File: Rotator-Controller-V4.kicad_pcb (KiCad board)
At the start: 2 copper layers, 99 x 70 mm, 91 parts, among them J1 Serial, J2 Rotator, J3 USB-C 2.0 16P, J4 Motor Cap, J6 Header 1x3, SW1 CW, SW2 CW, U1 ATtiny1616-M, U2 AP2161W, U3 CPC1966, U4 CPC1966, U5 CPC1966, U6 ADUM3160, U7 FT231XQ, U8 NDP6802SF-50

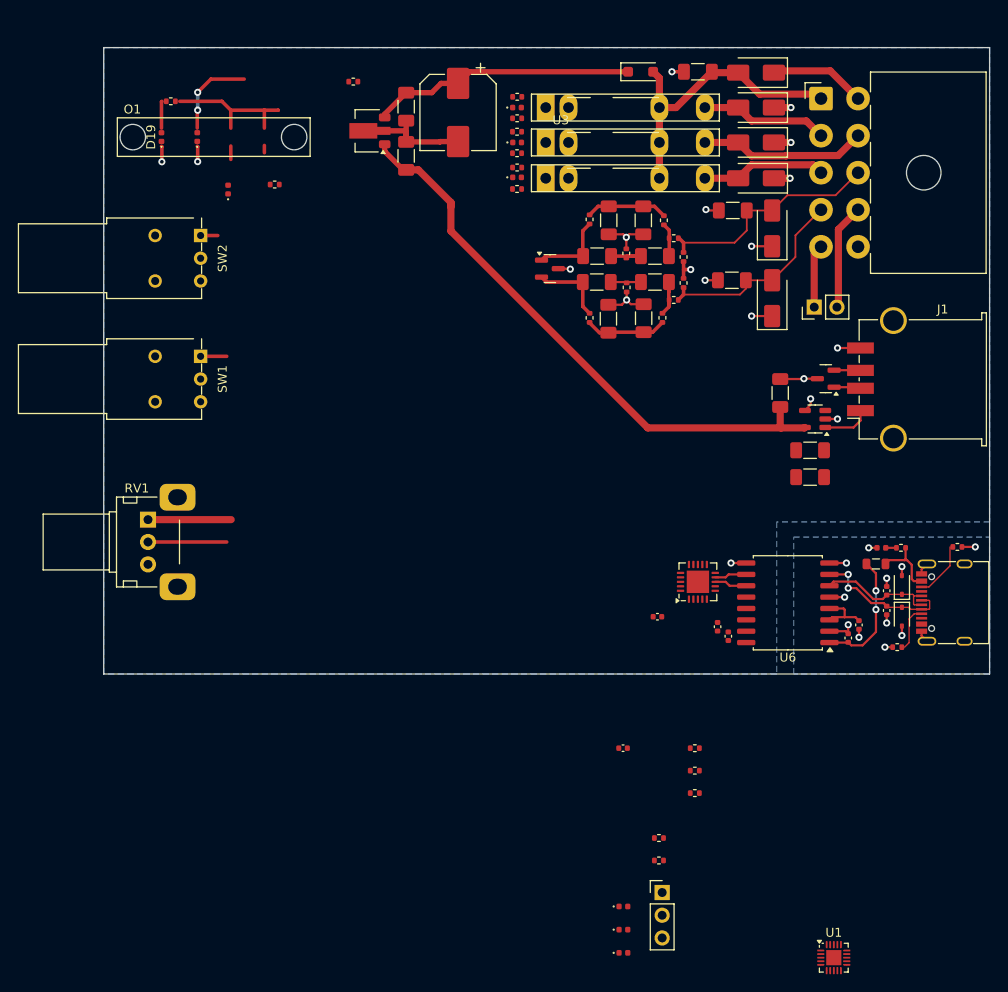
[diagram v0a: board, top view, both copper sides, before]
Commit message: More work on schematic Started software conversion to STM32F405 MCU
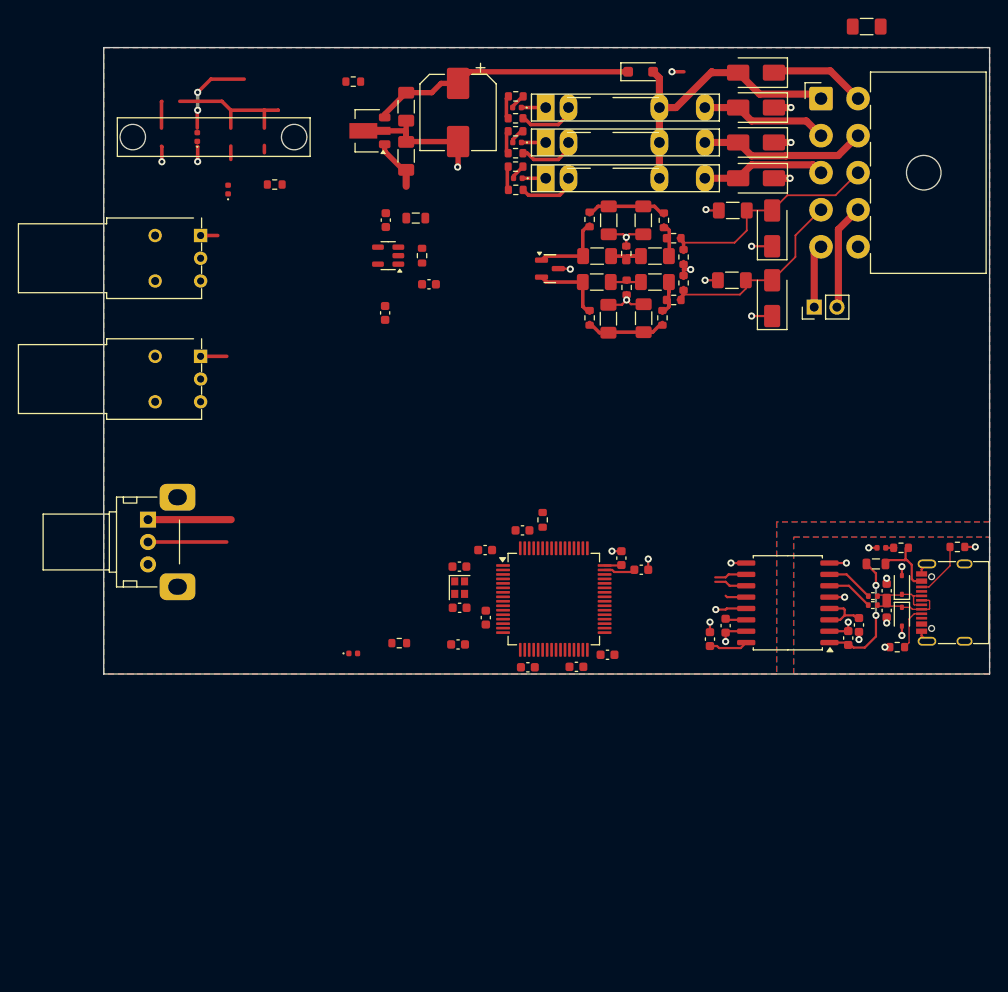
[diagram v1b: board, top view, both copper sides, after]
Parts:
- removed the C1 at (161.4, 57.7)
- removed the C19 at (156.9, 118.6)
- removed D19: 5V, LED_SMD:LED_0402_1005Metric
- removed D20, D21: Yellow, LED_SMD:LED_0402_1005Metric
- removed the D9 at (175.7, 92.0)
- removed the J1 at (185.9, 92.1)
- removed J6: Header 1x3, Connector_PinHeader_2.54mm:PinHeader_1x03_P2.54mm_Vertical
- removed the R15 at (102.5, 61.0)
- removed R27, R28, R29: 1K, Resistor_SMD:R_0402_1005Metric
- removed the U1 at (176.6, 156.7)
- added C11: 1u, Capacitor_SMD:C_0603_1608Metric, F.Cu at (141.8, 109.0)
- added C12: 10u, Capacitor_SMD:C_0603_1608Metric, F.Cu at (151.3, 122.8)
- added C16: 1u, Capacitor_SMD:C_0603_1608Metric, F.Cu at (152.8, 112.0)
- added C17: 10u, Capacitor_SMD:C_0603_1608Metric, F.Cu at (126.5, 74.3)
- added C18: 0.1u, Capacitor_SMD:C_0603_1608Metric, F.Cu at (137.7, 118.7)
- added C29: 0.1 200V, Capacitor_SMD:C_1206_3216Metric_Pad1.33x1.80mm_HandSolder, F.Cu at (180.3, 52.6)
- added C33: 10u, Capacitor_SMD:C_0603_1608Metric, F.Cu at (126.5, 84.7)
- added C34: 1u, Capacitor_SMD:C_0603_1608Metric, F.Cu at (131.3, 81.5)
- added C5: 10u, Capacitor_SMD:C_0603_1608Metric, F.Cu at (134.6, 121.7)
- added C6: 0.1u, Capacitor_SMD:C_0603_1608Metric, F.Cu at (137.6, 111.2)
- added C8: 1u, Capacitor_SMD:C_0603_1608Metric, F.Cu at (142.4, 124.2)
- added FB2: FerriteBead_Small, Inductor_SMD:L_0805_2012Metric, F.Cu at (129.9, 74.0)
- added R5: 27, Resistor_SMD:R_0402_1005Metric, F.Cu at (180.9, 117.3)
- added R6: 27, Resistor_SMD:R_0402_1005Metric, F.Cu at (181.0, 116.3)
- added R8: 10K, Resistor_SMD:R_0603_1608Metric, F.Cu at (144.1, 107.8)
- added Y1: 12M, Crystal:Crystal_SMD_2016-4Pin_2.0x1.6mm, F.Cu at (134.8, 115.3)
- C1: renamed from C16; footprint Capacitor_SMD:C_0402_1005Metric -> Capacitor_SMD:C_0603_1608Metric
- C10, C13: value 0.1 -> 20p; footprint Capacitor_SMD:C_1206_3216Metric_Pad1.33x1.80mm_HandSolder -> Capacitor_SMD:C_0603_1608Metric
- C14: value 120u -> 1u; footprint Capacitor_SMD:C_1206_3216Metric_Pad1.33x1.80mm_HandSolder -> Capacitor_SMD:C_0603_1608Metric
- C15: value .1u -> 10u; footprint Capacitor_SMD:C_0402_1005Metric -> Capacitor_SMD:C_0603_1608Metric
- C2: renamed from C20; footprint Capacitor_SMD:C_0402_1005Metric -> Capacitor_SMD:C_0603_1608Metric
- C3: renamed from C18; footprint Capacitor_SMD:C_0402_1005Metric -> Capacitor_SMD:C_0603_1608Metric
- C4: renamed from C25; footprint Capacitor_SMD:C_0402_1005Metric -> Capacitor_SMD:C_0603_1608Metric
- C7: renamed from C24; footprint Capacitor_SMD:C_0402_1005Metric -> Capacitor_SMD:C_0603_1608Metric
- C9: renamed from C17; footprint Capacitor_SMD:C_0402_1005Metric -> Capacitor_SMD:C_0603_1608Metric
- D16: renamed from D14; value SMAJ90CA -> SMAJ10CA
- D17: renamed from D15; value SMAJ90CA -> SMAJ10CA
- D4: renamed from D10; value White -> 5V_GRN
- R1: renamed from R10; footprint Resistor_SMD:R_0402_1005Metric -> Resistor_SMD:R_0603_1608Metric
- R10: renamed from R5; footprint Resistor_SMD:R_0402_1005Metric -> Resistor_SMD:R_0603_1608Metric
- R11: renamed from R20; value 1K5 -> 1K; footprint Resistor_SMD:R_0402_1005Metric -> Resistor_SMD:R_0603_1608Metric
- R12: renamed from R3; value 1k5 -> 1k; footprint Resistor_SMD:R_0402_1005Metric -> Resistor_SMD:R_0603_1608Metric
- R13: renamed from R19; value 1K5 -> 1K; footprint Resistor_SMD:R_0402_1005Metric -> Resistor_SMD:R_0603_1608Metric
- R14: renamed from R16; value 1K5 -> 1K; footprint Resistor_SMD:R_0402_1005Metric -> Resistor_SMD:R_0603_1608Metric
- R15: renamed from R18; value 1K5 -> 1K; footprint Resistor_SMD:R_0402_1005Metric -> Resistor_SMD:R_0603_1608Metric
- R16: renamed from R17; value 1K5 -> 1K; footprint Resistor_SMD:R_0402_1005Metric -> Resistor_SMD:R_0603_1608Metric
- R17: renamed from R1; footprint Resistor_SMD:R_0402_1005Metric -> Resistor_SMD:R_0603_1608Metric
- R18: renamed from R6; footprint Resistor_SMD:R_0402_1005Metric -> Resistor_SMD:R_0603_1608Metric
- R19: renamed from R8; footprint Resistor_SMD:R_0402_1005Metric -> Resistor_SMD:R_0603_1608Metric
- R2: renamed from R21; footprint Resistor_SMD:R_0402_1005Metric -> Resistor_SMD:R_0603_1608Metric
- R20: renamed from R7; footprint Resistor_SMD:R_0402_1005Metric -> Resistor_SMD:R_0603_1608Metric
- R21: renamed from R9; footprint Resistor_SMD:R_0402_1005Metric -> Resistor_SMD:R_0603_1608Metric
- R22: renamed from R11; footprint Resistor_SMD:R_0402_1005Metric -> Resistor_SMD:R_0603_1608Metric
- R23: renamed from R12; footprint Resistor_SMD:R_0402_1005Metric -> Resistor_SMD:R_0603_1608Metric
- R24: renamed from R13; footprint Resistor_SMD:R_0402_1005Metric -> Resistor_SMD:R_0603_1608Metric
- R25: renamed from R14; footprint Resistor_SMD:R_0402_1005Metric -> Resistor_SMD:R_0603_1608Metric
- R26: value 1K -> 10K; footprint Resistor_SMD:R_0402_1005Metric -> Resistor_SMD:R_0603_1608Metric
- R3: renamed from R22; footprint Resistor_SMD:R_0402_1005Metric -> Resistor_SMD:R_0603_1608Metric
- R4: renamed from R2; footprint Resistor_SMD:R_0402_1005Metric -> Resistor_SMD:R_0603_1608Metric
- R7: renamed from R25; footprint Resistor_SMD:R_0402_1005Metric -> Resistor_SMD:R_0603_1608Metric
- R9: renamed from R4; footprint Resistor_SMD:R_0402_1005Metric -> Resistor_SMD:R_0603_1608Metric
- U2: value AP2161W -> STM32F405RGTx; footprint Package_TO_SOT_SMD:SOT-23-5 -> Package_QFP:LQFP-64_10x10mm_P0.5mm
- U7: value FT231XQ -> AP2112K-3.3; footprint Package_DFN_QFN:QFN-20-1EP_4x4mm_P0.5mm_EP2.5x2.5mm -> Package_TO_SOT_SMD:SOT-23-5
- moved R26 72.6 mm to (130.6, 78.2), turned to 90 degrees
- moved U7 50.3 mm to (126.8, 78.2), turned to 180 degrees
- moved C13 41.8 mm to (134.8, 117.6), turned to 0 degrees
- moved D5 41.4 mm to (122.9, 122.7)
- moved C10 40.8 mm to (134.8, 113.0), turned to 0 degrees
- moved R7 36.3 mm to (128.0, 121.5)
- moved C14 35.6 mm to (147.8, 124.2)
- moved U2 35.5 mm to (145.3, 116.6), turned to 0 degrees
- moved C15 20.0 mm to (155.1, 113.3)
- moved R13 2.51 mm to (141.0, 68.3)
- moved R14 2.50 mm to (141.1, 70.9)
- moved C9 2.07 mm to (162.8, 121.1)
- moved C7 0.91 mm to (164.5, 119.6)
- moved R16 0.17 mm to (141.0, 62.9)
- moved R11 0.17 mm to (141.0, 64.3)
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- renumbered C21 to C19, C2 to C20, C3 to C21, C4 to C22, C5 to C23, C6 to C24, C7 to C25, C23 to C26, C8 to C27, C9 to C28, C22 to C30, C11 to C31, C12 to C32, D8 to D1, D13 to D10, D5 to D11, D3 to D12, D18 to D13, D17 to D14, D16 to D15, D11 to D2, D7 to D3, D12 to D5, D1 to D6, D4 to D7, D6 to D8, D2 to D9, J3 to J1, J4 to J2, J2 to J3, U6 to U1, U8 to U6
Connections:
- net /5VD renamed /VBUS
- C1 pad 1: Net-(D11-K) -> Net-(D2-K)
- C10 pad 1: /5V -> Net-(U2-PH0)
- C13 pad 1: /5V_Serial -> Net-(U2-PH1)
- C14 pad 1: /5V_Serial -> /+3V3
- C15 pad 1: /5V -> Net-(U2-VCAP_2)
- C3 pad 1: Net-(D8-K) -> Net-(D1-K)
- C7 pad 1: Net-(U6-PIN) -> /+3v3
- C9 pad 1: /5V -> /+3v3
- D1 pad 1: Net-(D8-K) -> Net-(D1-K)
- D12 pad 1: /Return -> GND
- D2 pad 1: Net-(D11-K) -> Net-(D2-K)
- J1 pad A6: Net-(D8-K) -> Net-(D1-K)
- J1 pad A7: Net-(D11-K) -> Net-(D2-K)
- J1 pad B6: Net-(D8-K) -> Net-(D1-K)
- J1 pad B7: Net-(D11-K) -> Net-(D2-K)
- J3 pad 10: /Return -> GND
- J3 pad 6: /Return -> GND
- R24 pad 1: /3V3 -> /+3V3
- R25 pad 1: /3V3 -> /+3V3
- R26 pad 1: /RXLED/ -> /5V
- R26 pad 2: Net-(D20-K) -> Net-(U7-EN)
- U1 pad 10: /D-M -> /D-
- U1 pad 11: /D+M -> /D+
- U1 pad 12: Net-(U6-PIN) -> /+3v3
- U1 pad 14: Net-(U6-PIN) -> /+3v3
- U1 pad 16: /5V -> /+3v3
- U1 pad 6: Net-(D8-K) -> Net-(U1-UD-)
- U1 pad 7: Net-(D11-K) -> Net-(U1-UD+)
- U2 pad 1: /5V_Serial -> unconnected-(U2-VBAT-Pad1)
- U2 pad 2: GND -> unconnected-(U2-PC13-Pad2)
- U2 pad 4: GND -> unconnected-(U2-PC15-Pad4)
- U2 pad 5: /5V -> Net-(U2-PH0)
- U7 pad 1: /RXD_U -> /5V
- U7 pad 2: unconnected-(U7-~{RI}-Pad2) -> GND
- U7 pad 3: GND -> Net-(U7-EN)
- U7 pad 5: unconnected-(U7-~{DCD}-Pad5) -> /+3v3
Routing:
- net /5V: track 65.3 -> 21.3 mm
- net GND: track 54.7 -> 77.7 mm, vias 19 -> 21
- net Net-(D11-K): track 15.5 -> 0.00 mm, vias 2 -> 0
- net Net-(D8-K): track 13.5 -> 0.00 mm
- net (no net): track 16.9 -> 4.52 mm
- net /Return: track 10.8 -> 0.00 mm
- net /+3v3: track 0.00 -> 9.13 mm
- net Net-(D2-K): track 0.00 -> 7.84 mm
- net Net-(D1-K): track 0.00 -> 6.97 mm
- net Net-(R14-Pad2): track 0.00 -> 6.63 mm
- net Net-(R12-Pad2): track 0.00 -> 6.45 mm
- net Net-(R16-Pad2): track 0.00 -> 6.44 mm
- net /5V_Serial: track 5.46 -> 0.00 mm
- net Net-(U1-UD+): track 0.00 -> 5.36 mm
- net Net-(U1-UD-): track 0.00 -> 5.23 mm
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- added copper zone on F.Cu, net GND
- added copper zone on F.Cu, net GNDD
